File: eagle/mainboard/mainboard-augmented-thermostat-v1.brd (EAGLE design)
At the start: 101.6 x 57.1 mm, 12 parts, among them Q1 RS485-ADAPTER0.05-CONNECTOR, X1 RJ45-6L21-B

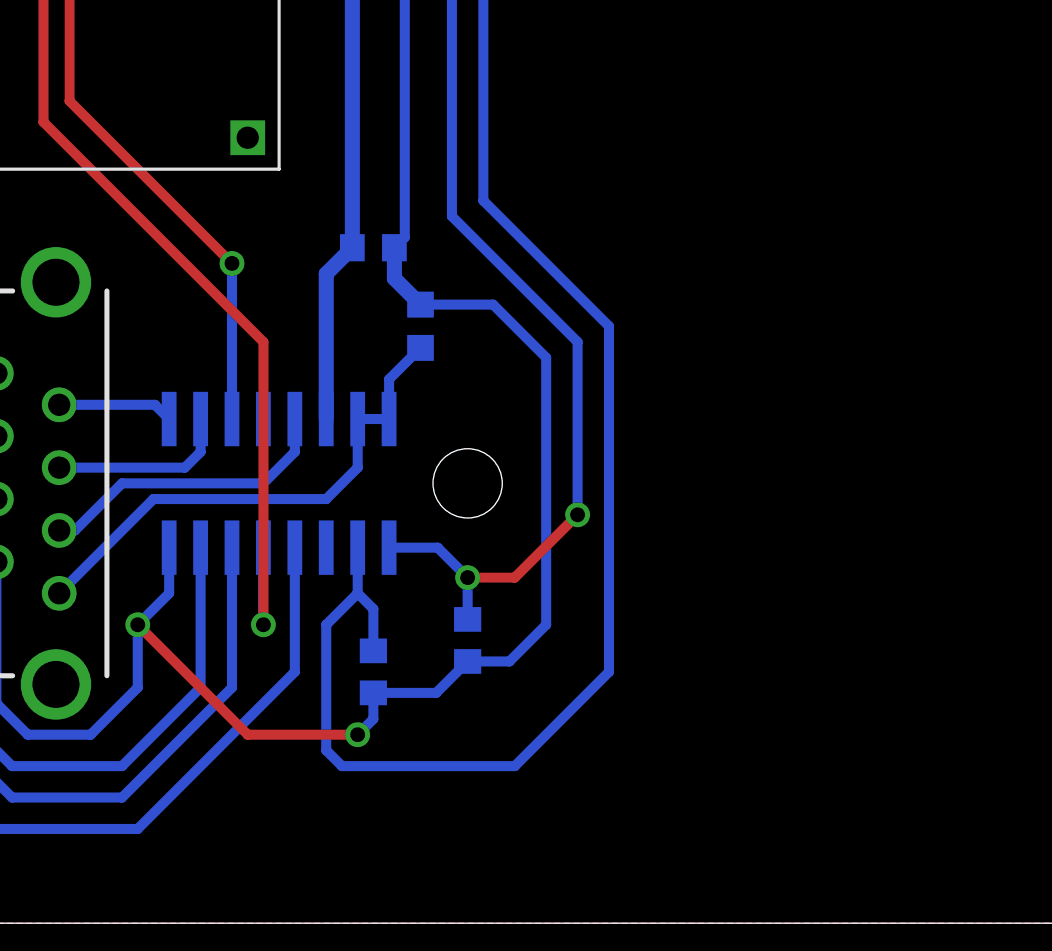
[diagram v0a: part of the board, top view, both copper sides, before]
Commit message: Added fourth DMP180 sensor, right on the mainboard, so that we can compare to ambient pressure, if we need to.
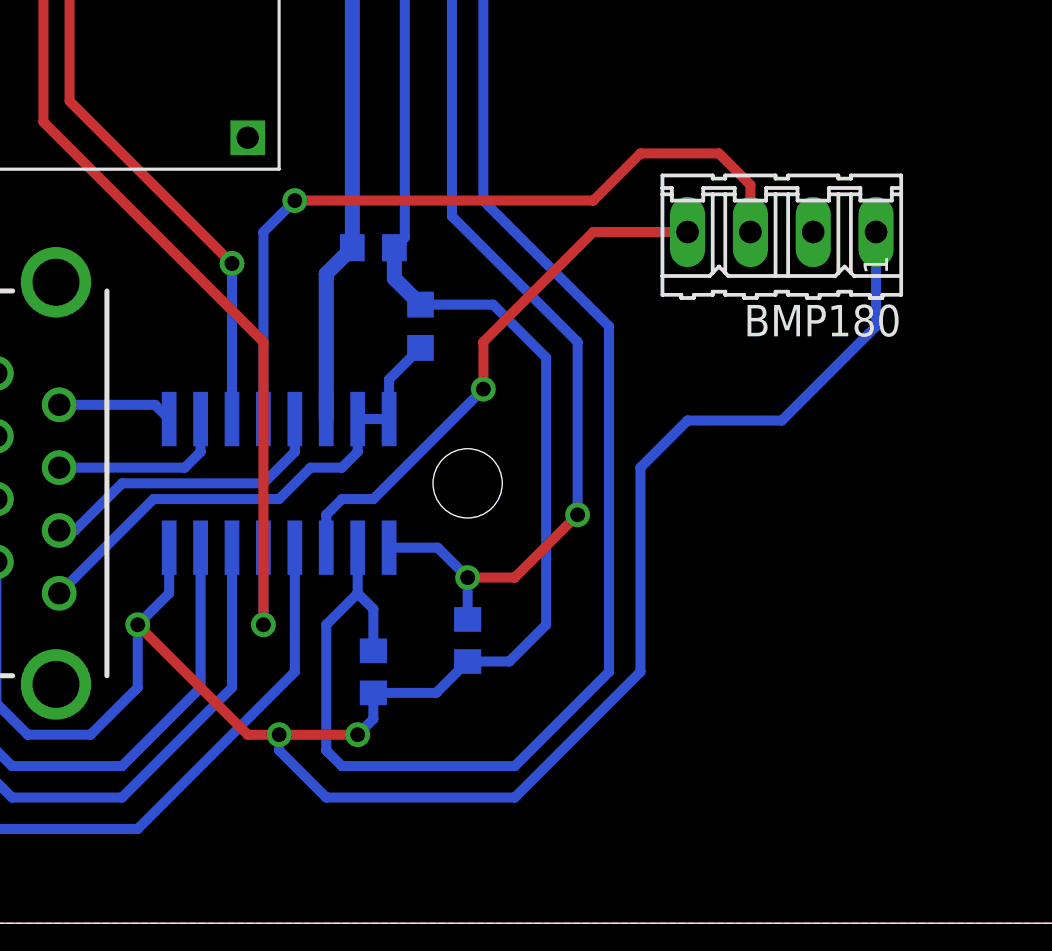
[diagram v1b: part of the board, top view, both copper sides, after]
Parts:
- added BMP180: (no value), con-amp-quick:04P
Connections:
- new net 1Y3: BMP180.4, U$2.11
- new net 2Y3: BMP180.3, U$2.4
- net +3V3: now also BMP180.1
- net GND: now also BMP180.2
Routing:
- net +3V3: track 99.9 -> 142.0 mm, vias 2 -> 3
- net 2Y3: track 0.00 -> 31.0 mm, vias 0 -> 1
- net 1Y3: track 0.00 -> 21.8 mm, vias 0 -> 1
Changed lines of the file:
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@@
 <element name="R2" library="adafruit" package="R0603" value="2k2" x="15.24" y="49.53"/>
 <element name="U$3" library="serge" package="MINI-BUCK-CONVERTER" value="MINI-BUCK-CONVERTER" x="22.86" y="30.48" rot="R90"/>
+<element name="BMP180" library="con-amp-quick" package="04P" value="" x="43.18" y="27.94" rot="R180">
+<attribute name="OC_FARNELL" value="unknown" x="43.18" y="27.94" size="1.778" layer="27" rot="R180" display="off"/>
+<attribute name="MPN" value="" x="43.18" y="27.94" size="1.778" layer="27" rot="R180" display="off"/>
+<attribute name="MF" value="" x="43.18" y="27.94" size="1.778" layer="27" rot="R180" display="off"/>
+<attribute name="OC_NEWARK" value="unknown" x="43.18" y="27.94" size="1.778" layer="27" rot="R180" display="off"/>
+</element>
 </elements>
 <signals>
@@
 <wire x1="26.035" y1="20.38" x2="27.305" y2="20.38" width="0.4064" layer="16"/>
 <wire x1="13.97" y1="13.335" x2="17.78" y2="17.145" width="0.4064" layer="16"/>
-<wire x1="17.78" y1="17.145" x2="24.765" y2="17.145" width="0.4064" layer="16"/>
-<wire x1="24.765" y1="17.145" x2="26.035" y2="18.415" width="0.4064" layer="16"/>
-<wire x1="26.035" y1="18.415" x2="26.035" y2="20.38" width="0.4064" layer="16"/>
 <polygon width="0.8128" layer="16">
 <vertex x="0" y="57.15"/>
@@
 <vertex x="0" y="0"/>
 </polygon>
+<contactref element="BMP180" pad="2"/>
+<wire x1="26.035" y1="19.05" x2="26.035" y2="20.38" width="0.4064" layer="16"/>
+<wire x1="17.78" y1="17.145" x2="22.86" y2="17.145" width="0.4064" layer="16"/>
+<wire x1="22.86" y1="17.145" x2="24.13" y2="18.415" width="0.4064" layer="16"/>
+<wire x1="24.13" y1="18.415" x2="25.4" y2="18.415" width="0.4064" layer="16"/>
+<wire x1="25.4" y1="18.415" x2="26.035" y2="19.05" width="0.4064" layer="16"/>
 </signal>
 <signal name="+12V">
@@
 <wire x1="26.67" y1="8.255" x2="26.035" y2="7.62" width="0.4064" layer="16"/>
 <via x="26.035" y="7.62" extent="1-16" drill="0.6" shape="square"/>
-<wire x1="26.035" y1="7.62" x2="21.59" y2="7.62" width="0.4064" layer="1"/>
+<wire x1="26.035" y1="7.62" x2="22.86" y2="7.62" width="0.4064" layer="1"/>
+<wire x1="22.86" y1="7.62" x2="21.59" y2="7.62" width="0.4064" layer="1"/>
 <wire x1="21.59" y1="7.62" x2="17.145" y2="12.065" width="0.4064" layer="1"/>
 <via x="17.145" y="12.065" extent="1-16" drill="0.6" shape="square"/>
@@
 <wire x1="30.48" y1="10.58" x2="32.17" y2="10.58" width="0.4064" layer="16"/>
 <wire x1="32.17" y1="10.58" x2="33.655" y2="12.065" width="0.4064" layer="16"/>
+<contactref element="BMP180" pad="1"/>
+<wire x1="46.99" y1="27.94" x2="46.99" y2="24.13" width="0.4064" layer="16"/>
+<wire x1="46.99" y1="24.13" x2="43.18" y2="20.32" width="0.4064" layer="16"/>
+<wire x1="43.18" y1="20.32" x2="39.37" y2="20.32" width="0.4064" layer="16"/>
+<wire x1="39.37" y1="20.32" x2="37.465" y2="18.415" width="0.4064" layer="16"/>
+<wire x1="37.465" y1="18.415" x2="37.465" y2="10.16" width="0.4064" layer="16"/>
+<wire x1="37.465" y1="10.16" x2="32.385" y2="5.08" width="0.4064" layer="16"/>
+<wire x1="32.385" y1="5.08" x2="24.765" y2="5.08" width="0.4064" layer="16"/>
+<wire x1="24.765" y1="5.08" x2="22.86" y2="6.985" width="0.4064" layer="16"/>
+<via x="22.86" y="7.62" extent="1-16" drill="0.6" shape="square"/>
+<wire x1="22.86" y1="7.62" x2="22.86" y2="6.985" width="0.4064" layer="16"/>
 <wire x1="16.09" y1="49.53" x2="8.04" y2="50.165" width="0" layer="19" extent="1-1"/>
 </signal>
+<signal name="2Y3">
+<contactref element="BMP180" pad="3"/>
+<contactref element="U$2" pad="4"/>
+<wire x1="22.225" y1="20.38" x2="22.225" y2="27.94" width="0.4064" layer="16"/>
+<wire x1="22.225" y1="27.94" x2="23.495" y2="29.21" width="0.4064" layer="16"/>
+<via x="23.495" y="29.21" extent="1-16" drill="0.6" shape="square"/>
+<wire x1="23.495" y1="29.21" x2="35.56" y2="29.21" width="0.4064" layer="1"/>
+<wire x1="35.56" y1="29.21" x2="37.465" y2="31.115" width="0.4064" layer="1"/>
+<wire x1="37.465" y1="31.115" x2="40.64" y2="31.115" width="0.4064" layer="1"/>
+<wire x1="40.64" y1="31.115" x2="41.91" y2="29.845" width="0.4064" layer="1"/>
+<wire x1="41.91" y1="29.845" x2="41.91" y2="27.94" width="0.4064" layer="1"/>
+</signal>
+<signal name="1Y3">
+<contactref element="BMP180" pad="4"/>
+<contactref element="U$2" pad="11"/>
+<wire x1="24.765" y1="15.18" x2="24.765" y2="16.51" width="0.4064" layer="16"/>
+<wire x1="24.765" y1="16.51" x2="25.4" y2="17.145" width="0.4064" layer="16"/>
+<wire x1="25.4" y1="17.145" x2="26.67" y2="17.145" width="0.4064" layer="16"/>
+<wire x1="26.67" y1="17.145" x2="31.115" y2="21.59" width="0.4064" layer="16"/>
+<via x="31.115" y="21.59" extent="1-16" drill="0.6" shape="square"/>
+<wire x1="31.115" y1="21.59" x2="31.115" y2="23.495" width="0.4064" layer="1"/>
+<wire x1="31.115" y1="23.495" x2="35.56" y2="27.94" width="0.4064" layer="1"/>
+<wire x1="35.56" y1="27.94" x2="39.37" y2="27.94" width="0.4064" layer="1"/>
+</signal>
 </signals>

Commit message: Added buzzer to the mainboard. Ready for first prototype!
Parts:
- added R3: 2k2, adafruit:R0603
- added SG1: F/HGP, buzzer:F/HGP
- added T1: (no value), transistor:SOT23-BEC
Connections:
- new net N$1: R3.1, T1.B
- new net N$2: SG1.2, T1.C
- net +5V: now also SG1.1
- net 18: now also R3.2
- net GND: now also T1.E
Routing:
- net +5V: track 19.3 -> 67.0 mm, vias 0 -> 1
- net N$2: track 0.00 -> 45.3 mm, vias 0 -> 1
- net 18: track 0.00 -> 6.92 mm
- net N$1: track 0.00 -> 3.37 mm
